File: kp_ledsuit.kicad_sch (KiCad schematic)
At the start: 4 parts, among them SW1 SW_SPDT, U1 STM32F103C8Tx

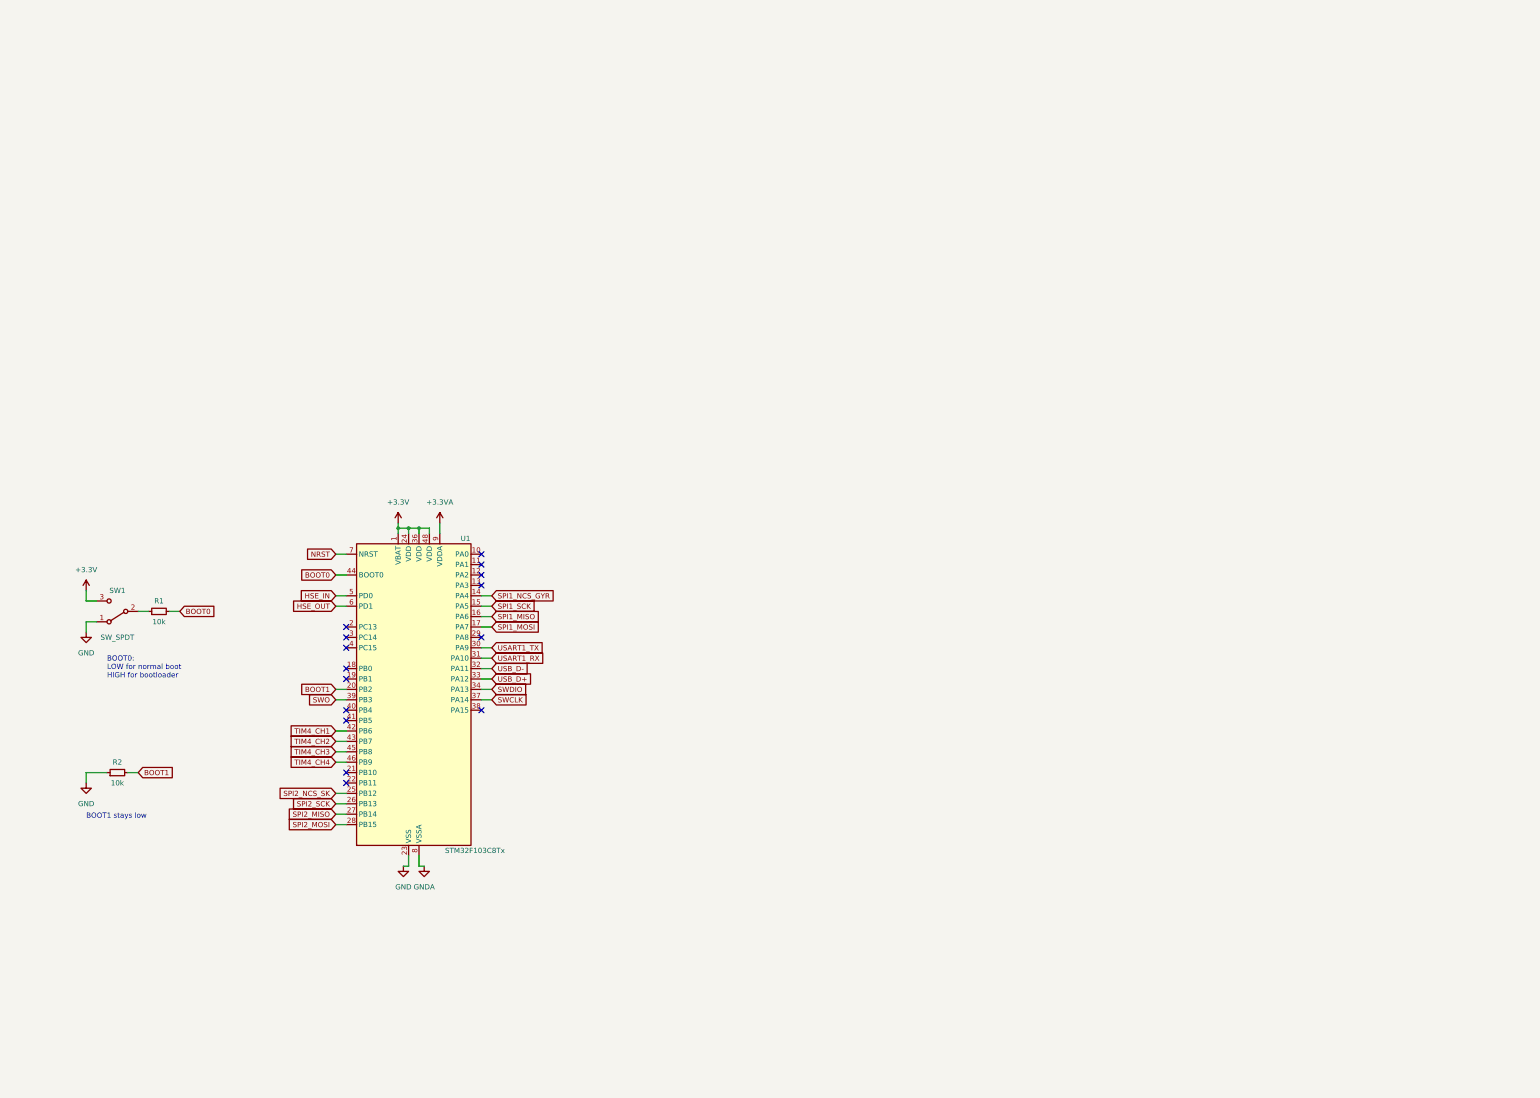
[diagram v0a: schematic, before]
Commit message: add power, usb, swd, onboard leds
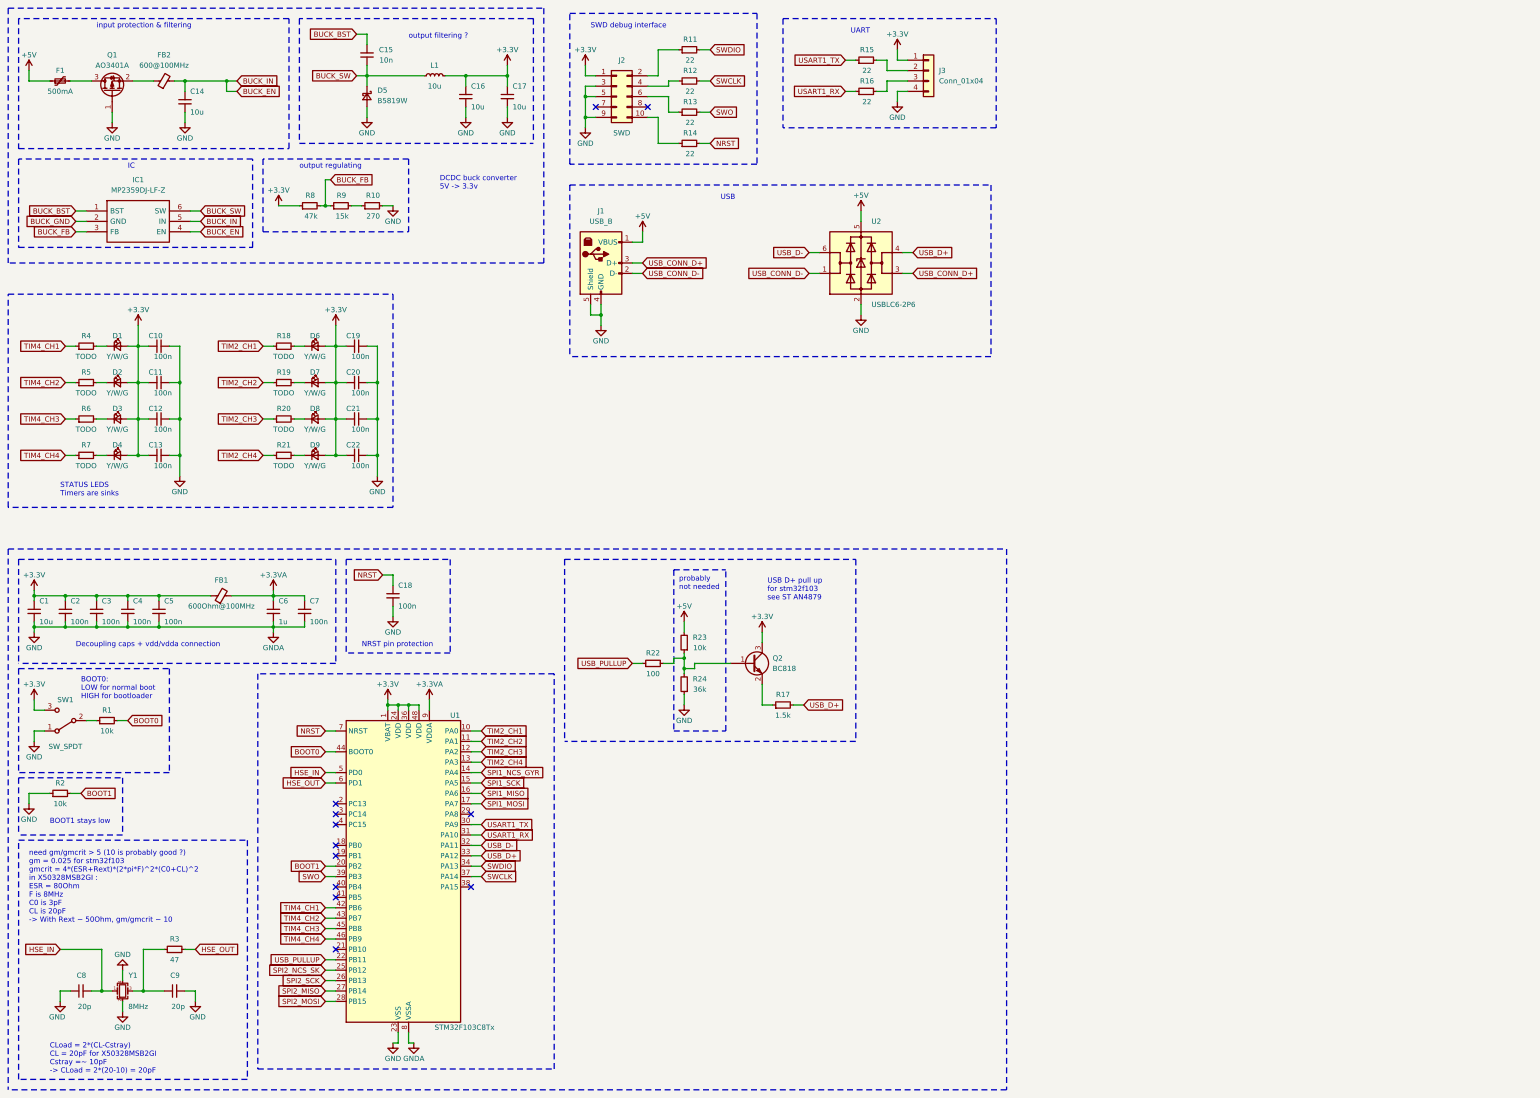
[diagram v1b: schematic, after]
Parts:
- added C1, C14, C16, C17: 10u, symbol Device:C_Small
- added C10, C11, C12, C13, C18, C19, C2, C20, C21, C22, C3, C4, C5, C7: 100n, symbol Device:C_Small
- added C15: 10n, symbol Device:C_Small
- added C6: 1u, symbol Device:C_Small
- added C8, C9: 20p, symbol Device:C_Small
- added D1, D2, D3, D4, D6, D7, D8, D9: Y/W/G, symbol Device:LED_Small
- added D5: B5819W, symbol Device:D_Schottky_Small
- added F1: 500mA, symbol Device:Polyfuse_Small
- added FB1: 600Ohm@100MHz, symbol Device:FerriteBead_Small
- added FB2: 600@100MHz, symbol Device:FerriteBead_Small
- added IC1: MP2359DJ-LF-Z, SOT95P280X100-6N, symbol SamacSys:MP2359DJ-LF-Z
- added J1: USB_B, symbol Connector:USB_B
- added J2: SWD, Connector_PCBEdge:Samtec_MECF-05-0_-NP-L-DV_2x05_P1.27mm_Edge, symbol Connector_Generic:Conn_02x05_Odd_Even
- added J3: Conn_01x04, symbol Connector_Generic:Conn_01x04
- added L1: 10u, symbol Device:L_Small
- added Q1: AO3401A, Package_TO_SOT_SMD:SOT-23, symbol Transistor_FET:AO3401A
- added Q2: BC818, Package_TO_SOT_SMD:SOT-23, symbol Transistor_BJT:BC818
- added R10: 270, symbol Device:R_Small
- added R11, R12, R13, R14, R15, R16: 22, symbol Device:R_Small
- added R17: 1.5k, symbol Device:R_Small
- added R18, R19, R20, R21, R4, R5, R6, R7: TODO, symbol Device:R_Small
- added R22: 100, symbol Device:R_Small
- added R23: 10k, symbol Device:R_Small
- added R24: 36k, symbol Device:R_Small
- added R3: 47, symbol Device:R_Small
- added R8: 47k, symbol Device:R_Small
- added R9: 15k, symbol Device:R_Small
- added U2: USBLC6-2P6, Package_TO_SOT_SMD:SOT-666, symbol Power_Protection:USBLC6-2P6
- added Y1: 8MHz, symbol Device:Crystal_GND24_Small
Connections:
- net GNDA is gone; now on net GND: U1.8 (VSSA)
- net +3.3V: now also C1.1, C10.2, C11.2, C12.2, C13.2, C16.1, C17.1, C19.2, C2.1, C20.2, C21.2, C22.2, C3.1, C4.1, C5.1, D1.2 (A), D2.2 (A), D3.2 (A), D4.2 (A), D6.2 (A), D7.2 (A), D8.2 (A), D9.2 (A), FB1.1, J2.1 (Pin_1), J3.1 (Pin_1), L1.2, Q2.3 (C), R8.1
- net +3.3VA: now also C6.1, C7.1, FB1.2
- net GND: now also C1.2, C10.1, C11.1, C12.1, C13.1, C14.2, C16.2, C17.2, C18.2, C19.1, C2.2, C20.1, C21.1, C22.1, C3.2, C4.2, C5.2, C6.2, C7.2, C8.1, C9.2, D5.2 (A), J1.4 (GND), J1.5 (Shield), J2.3 (Pin_3), J2.5 (Pin_5), J2.9 (Pin_9), J3.4 (Pin_4), Q1.1 (G), R10.2, R24.1, U2.2 (GND), Y1.2, Y1.4
- net HSE_IN: now also C8.2, Y1.1
- net HSE_OUT: now also R3.2
- net NRST: now also C18.1, R14.2
- net SWCLK: now also R12.2
- net SWDIO: now also R11.2
- net SWO: now also R13.2
- net TIM4_CH1: now also R4.1
- net TIM4_CH2: now also R5.1
- net TIM4_CH3: now also R6.1
- net TIM4_CH4: now also R7.1
- net USART1_RX: now also R16.1
- net USART1_TX: now also R15.1
- net USB_D+: now also R17.2, U2.4 (I/O2)
- net USB_D-: now also U2.6 (I/O1)
- net TIM2_CH1: now reaches U1.10 (PA0)
- net TIM2_CH1: now also R18.1
- net TIM2_CH2: now reaches U1.11 (PA1)
- net TIM2_CH2: now also R19.1
- net TIM2_CH3: now reaches U1.12 (PA2)
- net TIM2_CH3: now also R20.1
- net TIM2_CH4: now reaches U1.13 (PA3)
- net TIM2_CH4: now also R21.1
- net USB_PULLUP: now reaches U1.22 (PB11)
- net USB_PULLUP: now also R22.1
- new net: D8.1 (K), R20.2
- new net: J3.2 (Pin_2), R15.2
- new net: J3.3 (Pin_3), R16.2
- new net: D2.1 (K), R5.2
- new net: D6.1 (K), R18.2
- new net: C9.1, R3.1, Y1.3
- new net: J2.2 (Pin_2), R11.1
- new net: R10.1, R9.2
- new net: D7.1 (K), R19.2
- new net: FB2.1, Q1.2 (S)
- new net: F1.2, Q1.3 (D)
- new net: D4.1 (K), R7.2
- new net: D1.1 (K), R4.2
- new net: Q2.1 (B), R22.2, R23.1, R24.2
- new net: Q2.2 (E), R17.1
- new net: D9.1 (K), R21.2
- new net: J2.10 (Pin_10), R14.1
- new net: D3.1 (K), R6.2
- new net: J2.4 (Pin_4), R12.1
- new net: J2.6 (Pin_6), R13.1
- new net +5V: F1.1, J1.1 (VBUS), R23.2, U2.5 (VBUS)
- new net BUCK_BST: C15.2, IC1.1 (BST)
- new net BUCK_EN: C14.1, FB2.2, IC1.4 (EN), IC1.5 (IN)
- new net BUCK_FB: IC1.3 (FB), R8.2, R9.1
- new net BUCK_GND: IC1.2 (GND)
- new net BUCK_SW: C15.1, D5.1 (K), IC1.6 (SW), L1.1
- new net USB_CONN_D+: J1.3 (D+), U2.3 (I/O2)
- new net USB_CONN_D-: J1.2 (D-), U2.1 (I/O1)
- no-connect marks 15 -> 12
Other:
- note added: "CLoad = 2*(CL-Cstray) CL = 20pF for X50328MSB2GI Cstray =~ 10pF -> CLoad = 2*(20-10) = 20pF"
- note added: "DCDC buck converter 5V -> 3.3v"
- note added: "Decoupling caps + vdd/vdda connection"
- note added: "IC"
- note added: "NRST pin protection"
- note added: "STATUS LEDS Timers are sinks"
- note added: "SWD debug interface"
- note added: "UART"
- note added: "USB"
- note added: "USB D+ pull up for stm32f103 see ST AN4879"
- note added: "input protection & filtering"
- note added: "need gm/gmcrit > 5 (10 is probably good ?) gm = 0.025 for stm32f103 gmcrit = 4*(ESR+Rext)*(2*pi*F)^2*(C0+CL)^2 in X50328MSB2GI : ESR = 80Ohm F is 8MHz C0 is 3pF CL is 20pF -> With Rext ~ 50Ohm, gm/gmcrit ~ 10"
- note added: "output filtering ?"
- note added: "output regulating"
- note added: "probably not needed"
- moved on the sheet: R1, R2, SW1, U1

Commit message: add IMU & SKconn + move input protections to USB part
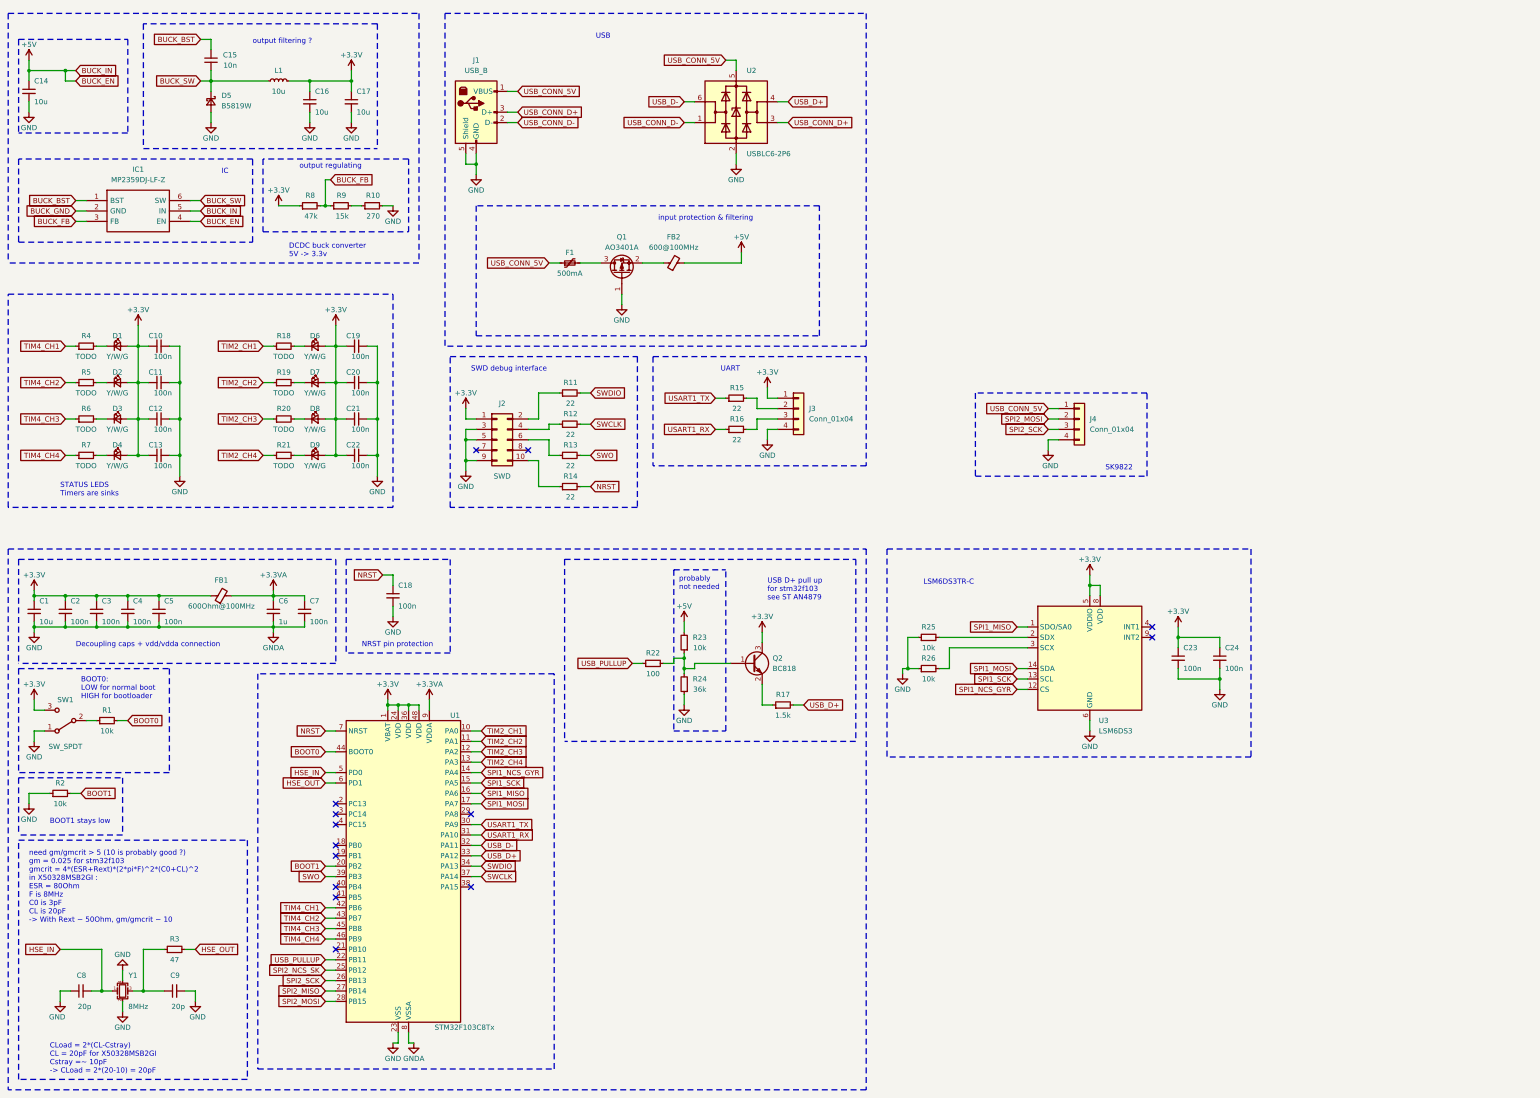
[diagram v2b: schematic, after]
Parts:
- added C23, C24: 100n, symbol Device:C_Small
- added J4: Conn_01x04, symbol Connector_Generic:Conn_01x04
- added R25, R26: 10k, symbol Device:R_Small
- added U3: LSM6DS3, Package_LGA:LGA-14_3x2.5mm_P0.5mm_LayoutBorder3x4y, symbol Sensor_Motion:LSM6DS3
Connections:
- net BUCK_EN is gone; now on net +5V: C14.1, FB2.2, IC1.4 (EN), IC1.5 (IN)
- net +3.3V: now also C23.1, C24.1, U3.5 (VDDIO), U3.8 (VDD)
- net +5V: no longer F1.1, J1.1 (VBUS), U2.5 (VBUS)
- net GND: now also C23.2, C24.2, J4.4 (Pin_4), R25.1, R26.1, U3.6 (GND), U3.7 (GND)
- net SPI1_MISO: now also U3.1 (SDO/SA0)
- net SPI1_MOSI: now also U3.14 (SDA)
- net SPI1_NCS_GYR: now also U3.12 (CS)
- net SPI1_SCK: now also U3.13 (SCL)
- net SPI2_MOSI: now also J4.2 (Pin_2)
- net SPI2_SCK: now also J4.3 (Pin_3)
- new net: R26.2, U3.3 (SCX)
- new net: R25.2, U3.2 (SDX)
- new net USB_CONN_5V: F1.1, J1.1 (VBUS), J4.1 (Pin_1), U2.5 (VBUS)
- no-connect marks 12 -> 14
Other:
- note added: "LSM6DS3TR-C"
- note added: "SK9822"
- moved on the sheet: C15, C16, C17, D5, IC1, J1, J2, J3, L1, R11, R12, R13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

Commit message: begin layout
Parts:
- removed J1: USB_B, symbol Connector:USB_B
- removed J3, J4: Conn_01x04, symbol Connector_Generic:Conn_01x04
- added H1, H2, H3, H4: M2, MountingHole:MountingHole_2.2mm_M2_Pad_Via, symbol Mechanical:MountingHole_Pad
- added J1: USB_B_Mini, Connector_USB:USB_Mini-B_Wuerth_65100516121_Horizontal, symbol Connector:USB_B_Mini
- added J3: Conn_01x04_MountingPin, Connector_Molex:Molex_PicoBlade_53261-0471_1x04-1MP_P1.25mm_Horizontal, symbol Connector_Generic_MountingPin:Conn_01x04_MountingPin
- added J4: SK9822, homemade_footprints:SK9822_edge_solder, symbol homemade_symbols:SK9822_solder_connector
- C1: renamed from C14; footprint (none) -> Capacitor_SMD:C_1206_3216Metric
- C10: renamed from C13; footprint (none) -> Capacitor_SMD:C_0402_1005Metric
- C11: renamed from C5; footprint (none) -> Capacitor_SMD:C_0402_1005Metric
- C12: renamed from C9; footprint (none) -> Capacitor_SMD:C_0402_1005Metric
- C13: renamed from C15; footprint (none) -> Capacitor_SMD:C_0603_1608Metric
- C14: renamed from C6; footprint (none) -> Capacitor_SMD:C_0805_2012Metric
- C15: renamed from C7; footprint (none) -> Capacitor_SMD:C_0402_1005Metric
- C16, C17: footprint (none) -> Capacitor_SMD:C_1206_3216Metric
- C18: renamed from C19; footprint (none) -> Capacitor_SMD:C_0402_1005Metric
- C19: renamed from C20; footprint (none) -> Capacitor_SMD:C_0402_1005Metric
- C2: renamed from C1; footprint (none) -> Capacitor_SMD:C_0805_2012Metric
- C20: renamed from C21; footprint (none) -> Capacitor_SMD:C_0402_1005Metric
- C21: renamed from C22; footprint (none) -> Capacitor_SMD:C_0402_1005Metric
- C22: renamed from C18; footprint (none) -> Capacitor_SMD:C_0402_1005Metric
- C23, C24: footprint (none) -> Capacitor_SMD:C_0402_1005Metric
- C3: renamed from C2; footprint (none) -> Capacitor_SMD:C_0402_1005Metric
- C4: renamed from C8; footprint (none) -> Capacitor_SMD:C_0402_1005Metric
- C5: renamed from C3; footprint (none) -> Capacitor_SMD:C_0402_1005Metric
- C6: renamed from C4; footprint (none) -> Capacitor_SMD:C_0402_1005Metric
- C7: renamed from C10; footprint (none) -> Capacitor_SMD:C_0402_1005Metric
- C8: renamed from C11; footprint (none) -> Capacitor_SMD:C_0402_1005Metric
- C9: renamed from C12; footprint (none) -> Capacitor_SMD:C_0402_1005Metric
- D1, D2, D3, D4, D6, D7, D8, D9: footprint (none) -> LED_SMD:LED_0805_2012Metric
- D5: footprint (none) -> Diode_SMD:D_SOD-123
- F1: footprint (none) -> Fuse:Fuse_1206_3216Metric
- FB1: value 600Ohm@100MHz -> 600@100MHz; footprint (none) -> Inductor_SMD:L_0805_2012Metric
- FB2: footprint (none) -> Inductor_SMD:L_0805_2012Metric
- IC1: footprint SOT95P280X100-6N -> SamacSys:SOT95P280X100-6N
- J2: footprint Connector_PCBEdge:Samtec_MECF-05-0_-NP-L-DV_2x05_P1.27mm_Edge -> Connector_PinSocket_1.27mm:PinSocket_2x05_P1.27mm_Vertical_SMD
- L1: footprint (none) -> Inductor_SMD:L_Sunlord_MWSA0503S
- R1: renamed from R2; footprint (none) -> Resistor_SMD:R_0603_1608Metric
- R10: renamed from R20; footprint (none) -> Resistor_SMD:R_0805_2012Metric
- R11: renamed from R21; footprint (none) -> Resistor_SMD:R_0805_2012Metric
- R12: renamed from R8; footprint (none) -> Resistor_SMD:R_1206_3216Metric
- R13: renamed from R9; footprint (none) -> Resistor_SMD:R_1206_3216Metric
- R14: renamed from R10; footprint (none) -> Resistor_SMD:R_1206_3216Metric
- R15: renamed from R11; footprint (none) -> Resistor_SMD:R_0402_1005Metric
- R16: renamed from R12; footprint (none) -> Resistor_SMD:R_0402_1005Metric
- R17: renamed from R13; footprint (none) -> Resistor_SMD:R_0402_1005Metric
- R18: renamed from R14; footprint (none) -> Resistor_SMD:R_0402_1005Metric
- R19: renamed from R22; footprint (none) -> Resistor_SMD:R_0603_1608Metric
- R2: renamed from R4; footprint (none) -> Resistor_SMD:R_0805_2012Metric
- R20: renamed from R23; footprint (none) -> Resistor_SMD:R_0603_1608Metric
- R21: renamed from R24; footprint (none) -> Resistor_SMD:R_0603_1608Metric
- R22: renamed from R15; footprint (none) -> Resistor_SMD:R_0402_1005Metric
- R23: renamed from R16; footprint (none) -> Resistor_SMD:R_0402_1005Metric
- R24: renamed from R17; footprint (none) -> Resistor_SMD:R_0603_1608Metric
- R25, R26: footprint (none) -> Resistor_SMD:R_0603_1608Metric
- R3: renamed from R5; footprint (none) -> Resistor_SMD:R_0805_2012Metric
- R4: renamed from R6; footprint (none) -> Resistor_SMD:R_0805_2012Metric
- R5: renamed from R7; footprint (none) -> Resistor_SMD:R_0805_2012Metric
- R6: renamed from R1; footprint (none) -> Resistor_SMD:R_0603_1608Metric
- R7: renamed from R3; footprint (none) -> Resistor_SMD:R_0402_1005Metric
- R8: renamed from R18; footprint (none) -> Resistor_SMD:R_0805_2012Metric
- R9: renamed from R19; footprint (none) -> Resistor_SMD:R_0805_2012Metric
- SW1: footprint (none) -> Button_Switch_SMD:SW_SPDT_PCM12
- Y1: value 8MHz -> 12MHz; footprint (none) -> Crystal:Crystal_SMD_3225-4Pin_3.2x2.5mm
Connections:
- net BUCK_GND is gone; now on net GND: IC1.2 (GND)
- net +3.3V: now also J3.1 (Pin_1)
- net GND: now also H1.1, H2.1, H3.1, H4.1, J1.5 (GND), J1.6 (Shield), J3.4 (Pin_4), J4.1 (GND)
- net SPI2_MOSI: now also J4.3 (DATA)
- net SPI2_SCK: now also J4.2 (CLOCK)
- net USB_CONN_5V: now also J1.1 (VBUS), J4.4 (+5V)
- net USB_CONN_D+: now also U2.6 (I/O1), J1.3 (D+); no longer U2.3 (I/O2)
- net USB_CONN_D-: now also U2.4 (I/O2), J1.2 (D-); no longer U2.1 (I/O1)
- net USB_D+: now also U2.1 (I/O1); no longer U2.4 (I/O2)
- net USB_D-: now also U2.3 (I/O2); no longer U2.6 (I/O1)
- net at R22.2: now also J3.2 (Pin_2)
- net at R23.2: now also J3.3 (Pin_3)
- net SPI2_MISO: no longer names the net of U1.27 (PB14)
- net SPI2_NCS_SK: no longer names the net of U1.25 (PB12)
- no-connect marks 14 -> 18
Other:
- note added: "mounting holes"

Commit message: WIP first proto layout: 1 face
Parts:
- D1, D2, D3, D4, D6, D7, D8, D9: JLCPCB Part # (none) -> C2297
- D5: JLCPCB Part # (none) -> C8598
- F1: JLCPCB Part # (none) -> C2984676
- FB1, FB2: JLCPCB Part # (none) -> C1017
- IC1: JLCPCB Part # (none) -> C18198375
- L1: JLCPCB Part # (none) -> C408412
- Q1: JLCPCB Part # (none) -> C15127
- U1: JLCPCB Part # (none) -> C8734
- U2: JLCPCB Part # (none) -> C15999
- U3: JLCPCB Part # (none) -> C967633
- Y1: JLCPCB Part # (none) -> C9002
